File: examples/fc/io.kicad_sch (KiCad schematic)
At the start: 8 parts, among them J4 MOTORS 1-4, J5 RX, J6 VTX, J7 GPS, J8 LED STRIP, Q1 2N7002

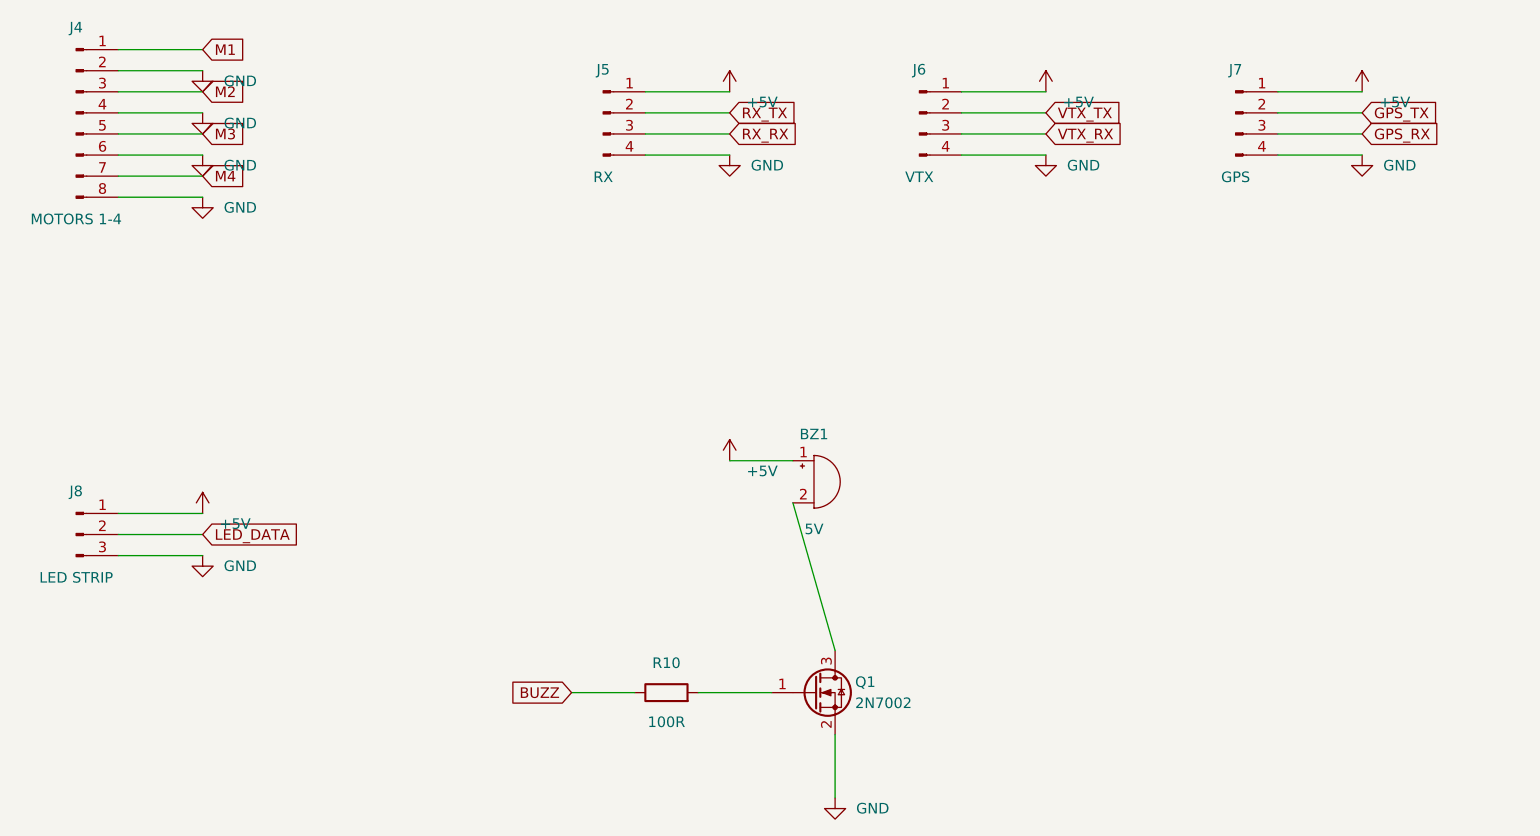
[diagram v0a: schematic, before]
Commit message: Add structured schematic scenes and fix example overlaps
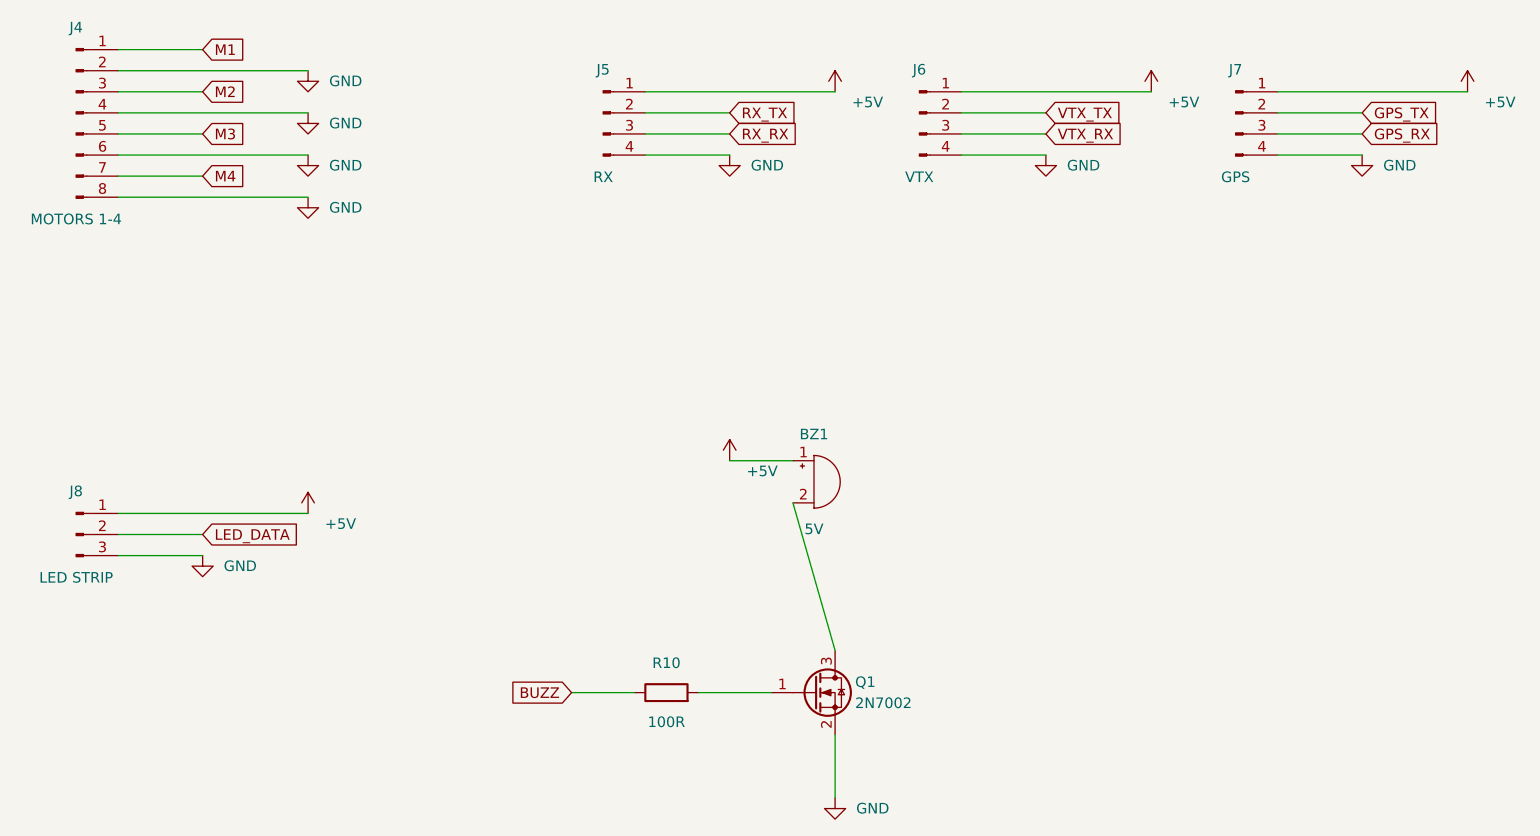
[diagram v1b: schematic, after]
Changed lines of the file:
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@@
 	(symbol
 		(lib_id "power:GND")
-		(at 78.74 83.82 0)
+		(at 91.44 83.82 0)
 		(unit 1)
 		(exclude_from_sim no)
@@
 		(dnp no)
 		(property "Reference" "#PWR0001"
-			(at 81.28 82.55 0)
+			(at 93.98 82.55 0)
 			(effects
 				(font
@@
 		)
 		(property "Value" "GND"
-			(at 81.28 85.09 0)
-			(effects
-				(font
-					(size 1.27 1.27)
-				)
-				(justify left)
-			)
-		)
-		(property "Footprint" ""
-			(at 78.74 83.82 0)
+			(at 93.98 85.09 0)
+			(effects
+				(font
+					(size 1.27 1.27)
+				)
+				(justify left)
+			)
+		)
+		(property "Footprint" ""
+			(at 91.44 83.82 0)
 			(effects
 				(font
@@
 	(symbol
 		(lib_id "power:GND")
-		(at 78.74 88.9 0)
+		(at 91.44 88.9 0)
 		(unit 1)
 		(exclude_from_sim no)
@@
 		(dnp no)
 		(property "Reference" "#PWR0002"
-			(at 81.28 87.63 0)
+			(at 93.98 87.63 0)
 			(effects
 				(font
@@
 		)
 		(property "Value" "GND"
-			(at 81.28 90.17 0)
-			(effects
-				(font
-					(size 1.27 1.27)
-				)
-				(justify left)
-			)
-		)
-		(property "Footprint" ""
-			(at 78.74 88.9 0)
+			(at 93.98 90.17 0)
+			(effects
+				(font
+					(size 1.27 1.27)
+				)
+				(justify left)
+			)
+		)
+		(property "Footprint" ""
+			(at 91.44 88.9 0)
 			(effects
 				(font
@@
 	(symbol
 		(lib_id "power:GND")
-		(at 78.74 93.98 0)
+		(at 91.44 93.98 0)
 		(unit 1)
 		(exclude_from_sim no)
@@
 		(dnp no)
 		(property "Reference" "#PWR0003"
-			(at 81.28 92.71 0)
+			(at 93.98 92.71 0)
 			(effects
 				(font
@@
 		)
 		(property "Value" "GND"
-			(at 81.28 95.25 0)
-			(effects
-				(font
-					(size 1.27 1.27)
-				)
-				(justify left)
-			)
-		)
-		(property "Footprint" ""
-			(at 78.74 93.98 0)
+			(at 93.98 95.25 0)
+			(effects
+				(font
+					(size 1.27 1.27)
+				)
+				(justify left)
+			)
+		)
+		(property "Footprint" ""
+			(at 91.44 93.98 0)
 			(effects
 				(font
@@
 	(symbol
 		(lib_id "power:GND")
-		(at 78.74 99.06 0)
+		(at 91.44 99.06 0)
 		(unit 1)
 		(exclude_from_sim no)
@@
 		(dnp no)
 		(property "Reference" "#PWR0004"
-			(at 81.28 97.79 0)
+			(at 93.98 97.79 0)
 			(effects
 				(font
@@
 		)
 		(property "Value" "GND"
-			(at 81.28 100.33 0)
-			(effects
-				(font
-					(size 1.27 1.27)
-				)
-				(justify left)
-			)
-		)
-		(property "Footprint" ""
-			(at 78.74 99.06 0)
+			(at 93.98 100.33 0)
+			(effects
+				(font
+					(size 1.27 1.27)
+				)
+				(justify left)
+			)
+		)
+		(property "Footprint" ""
+			(at 91.44 99.06 0)
 			(effects
 				(font
@@
 	(symbol
 		(lib_id "power:+5V")
-		(at 142.24 86.36 0)
+		(at 154.94 86.36 0)
 		(unit 1)
 		(exclude_from_sim no)
@@
 		(dnp no)
 		(property "Reference" "#PWR0005"
-			(at 144.272 85.09 0)
+			(at 156.972 85.09 0)
 			(effects
 				(font
@@
 		)
 		(property "Value" "+5V"
-			(at 144.272 87.63 0)
-			(effects
-				(font
-					(size 1.27 1.27)
-				)
-				(justify left)
-			)
-		)
-		(property "Footprint" ""
-			(at 142.24 86.36 0)
+			(at 156.972 87.63 0)
+			(effects
+				(font
+					(size 1.27 1.27)
+				)
+				(justify left)
+			)
+		)
+		(property "Footprint" ""
+			(at 154.94 86.36 0)
 			(effects
 				(font
@@
 	(symbol
 		(lib_id "power:+5V")
-		(at 180.34 86.36 0)
+		(at 193.04 86.36 0)
 		(unit 1)
 		(exclude_from_sim no)
@@
 		(dnp no)
 		(property "Reference" "#PWR0007"
-			(at 182.372 85.09 0)
+			(at 195.072 85.09 0)
 			(effects
 				(font
@@
 		)
 		(property "Value" "+5V"
-			(at 182.372 87.63 0)
-			(effects
-				(font
-					(size 1.27 1.27)
-				)
-				(justify left)
-			)
-		)
-		(property "Footprint" ""
-			(at 180.34 86.36 0)
+			(at 195.072 87.63 0)
+			(effects
+				(font
+					(size 1.27 1.27)
+				)
+				(justify left)
+			)
+		)
+		(property "Footprint" ""
+			(at 193.04 86.36 0)
 			(effects
 				(font
@@
 	(symbol
 		(lib_id "power:+5V")
-		(at 218.44 86.36 0)
+		(at 231.14 86.36 0)
 		(unit 1)
 		(exclude_from_sim no)
@@
 		(dnp no)
 		(property "Reference" "#PWR0009"
-			(at 220.472 85.09 0)
+			(at 233.172 85.09 0)
 			(effects
 				(font
@@
 		)
 		(property "Value" "+5V"
-			(at 220.472 87.63 0)
-			(effects
-				(font
-					(size 1.27 1.27)
-				)
-				(justify left)
-			)
-		)
-		(property "Footprint" ""
-			(at 218.44 86.36 0)
+			(at 233.172 87.63 0)
+			(effects
+				(font
+					(size 1.27 1.27)
+				)
+				(justify left)
+			)
+		)
+		(property "Footprint" ""
+			(at 231.14 86.36 0)
 			(effects
 				(font
@@
 	(symbol
 		(lib_id "power:+5V")
-		(at 78.74 137.16 0)
+		(at 91.44 137.16 0)
 		(unit 1)
 		(exclude_from_sim no)
@@
 		(dnp no)
 		(property "Reference" "#PWR0011"
-			(at 80.772 135.89 0)
+			(at 93.472 135.89 0)
 			(effects
 				(font
@@
 		)
 		(property "Value" "+5V"
-			(at 80.772 138.43 0)
-			(effects
-				(font
-					(size 1.27 1.27)
-				)
-				(justify left)
-			)
-		)
-		(property "Footprint" ""
-			(at 78.74 137.16 0)
+			(at 93.472 138.43 0)
+			(effects
+				(font
+					(size 1.27 1.27)
+				)
+				(justify left)
+			)
+		)
+		(property "Footprint" ""
+			(at 91.44 137.16 0)
 			(effects
 				(font
@@
 		(pts
 			(xy 68.58 83.82)
-			(xy 78.74 83.82)
+			(xy 91.44 83.82)
 		)
 		(stroke
@@
 		(pts
 			(xy 68.58 88.9)
-			(xy 78.74 88.9)
+			(xy 91.44 88.9)
 		)
 		(stroke
@@
 		(pts
 			(xy 68.58 93.98)
-			(xy 78.74 93.98)
+			(xy 91.44 93.98)
 		)
 		(stroke
@@
 		(pts
 			(xy 68.58 99.06)
-			(xy 78.74 99.06)
+			(xy 91.44 99.06)
 		)
 		(stroke
@@
 		(pts
 			(xy 132.08 86.36)
-			(xy 142.24 86.36)
+			(xy 154.94 86.36)
 		)
 		(stroke
@@
 		(pts
 			(xy 170.18 86.36)
-			(xy 180.34 86.36)
+			(xy 193.04 86.36)
 		)
 		(stroke
@@
 		(pts
 			(xy 208.28 86.36)
-			(xy 218.44 86.36)
+			(xy 231.14 86.36)
 		)
 		(stroke
@@
 		(pts
 			(xy 68.58 137.16)
-			(xy 78.74 137.16)
-		)
-		(stroke
+			(xy 91.44 137.16)
+		)
+		(stroke
